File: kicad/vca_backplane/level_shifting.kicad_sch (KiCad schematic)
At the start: 10 parts, among them Q3 BSS138, Q4 BSS138, U2 74HCT245, U3 74LVC245

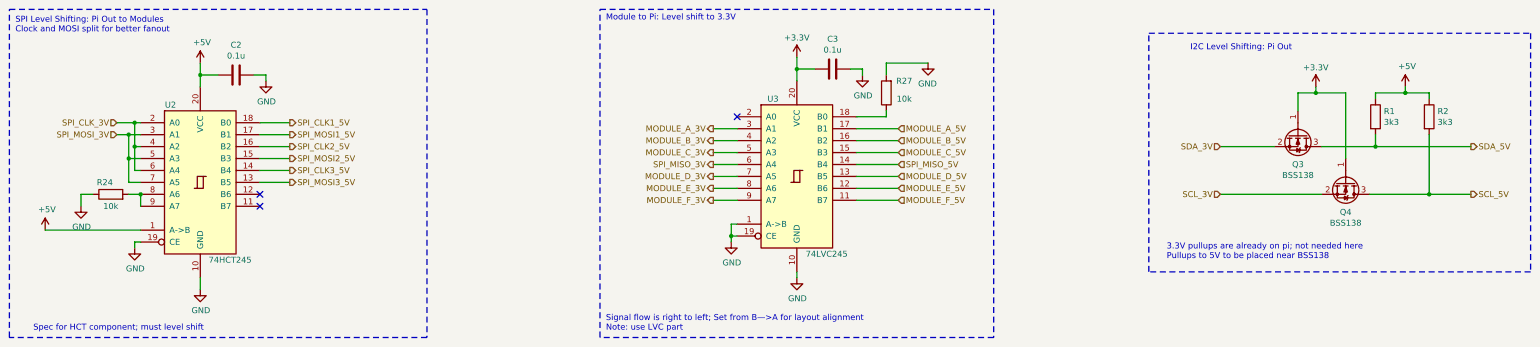
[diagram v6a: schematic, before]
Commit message: geographically reorientated from pcb
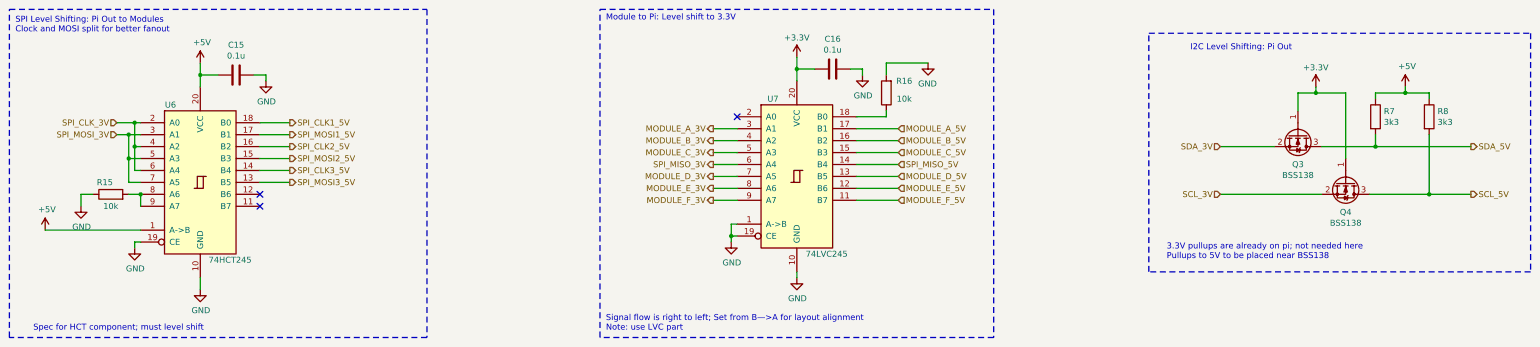
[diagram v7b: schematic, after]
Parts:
- renumbered C2 to C15, C3 to C16, R24 to R15, R27 to R16, R1 to R7, R2 to R8, U2 to U6, U3 to U7
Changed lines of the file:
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@@
   (symbol (lib_id "Device:C") (at 77.47 55.88 270) (unit 1)
     (in_bom yes) (on_board yes) (dnp no)
-    (property "Reference" "C2" (at 77.47 49.4792 90)
+    (property "Reference" "C15" (at 77.47 49.4792 90)
       (effects (font (size 1.27 1.27)))
     )
@@
       (project "vca_backplane"
         (path "/bdbd6910-8f28-459f-89ba-e6dd447d59a9/00000000-0000-0000-0000-00006255a619"
-          (reference "C2") (unit 1)
+          (reference "C15") (unit 1)
         )
       )
@@
   (symbol (lib_id "74xx:74HC245") (at 69.85 78.74 0) (unit 1)
     (in_bom yes) (on_board yes) (dnp no)
-    (property "Reference" "U2" (at 63.5 62.23 0)
+    (property "Reference" "U6" (at 63.5 62.23 0)
       (effects (font (size 1.27 1.27)))
     )
@@
       (project "vca_backplane"
         (path "/bdbd6910-8f28-459f-89ba-e6dd447d59a9/00000000-0000-0000-0000-00006255a619"
-          (reference "U2") (unit 1)
+          (reference "U6") (unit 1)
         )
       )
@@
   (symbol (lib_id "Device:R") (at 320.04 64.77 0) (unit 1)
     (in_bom yes) (on_board yes) (dnp no)
-    (property "Reference" "R1" (at 321.818 63.6016 0)
+    (property "Reference" "R7" (at 321.818 63.6016 0)
       (effects (font (size 1.27 1.27)) (justify left))
     )
@@
       (project "vca_backplane"
         (path "/bdbd6910-8f28-459f-89ba-e6dd447d59a9/00000000-0000-0000-0000-00006255a619"
-          (reference "R1") (unit 1)
+          (reference "R7") (unit 1)
         )
       )
@@
   (symbol (lib_id "Device:R") (at 331.47 64.77 0) (unit 1)
     (in_bom yes) (on_board yes) (dnp no)
-    (property "Reference" "R2" (at 333.248 63.6016 0)
+    (property "Reference" "R8" (at 333.248 63.6016 0)
       (effects (font (size 1.27 1.27)) (justify left))
     )
@@
       (project "vca_backplane"
         (path "/bdbd6910-8f28-459f-89ba-e6dd447d59a9/00000000-0000-0000-0000-00006255a619"
-          (reference "R2") (unit 1)
+          (reference "R8") (unit 1)
         )
       )
@@
   (symbol (lib_id "74xx:74HC245") (at 196.85 77.47 0) (unit 1)
     (in_bom yes) (on_board yes) (dnp no)
-    (property "Reference" "U3" (at 191.77 60.96 0)
+    (property "Reference" "U7" (at 191.77 60.96 0)
       (effects (font (size 1.27 1.27)))
     )
@@
       (project "vca_backplane"
         (path "/bdbd6910-8f28-459f-89ba-e6dd447d59a9/00000000-0000-0000-0000-00006255a619"
-          (reference "U3") (unit 1)
+          (reference "U7") (unit 1)
         )
       )
@@
   (symbol (lib_id "Device:C") (at 204.47 54.61 270) (unit 1)
     (in_bom yes) (on_board yes) (dnp no)
-    (property "Reference" "C3" (at 204.47 48.2092 90)
+    (property "Reference" "C16" (at 204.47 48.2092 90)
       (effects (font (size 1.27 1.27)))
     )
@@
       (project "vca_backplane"
         (path "/bdbd6910-8f28-459f-89ba-e6dd447d59a9/00000000-0000-0000-0000-00006255a619"
-          (reference "C3") (unit 1)
+          (reference "C16") (unit 1)
         )
       )
@@
   (symbol (lib_id "Device:R") (at 215.9 59.69 180) (unit 1)
     (in_bom yes) (on_board yes) (dnp no)
-    (property "Reference" "R27" (at 219.71 57.15 0)
+    (property "Reference" "R16" (at 219.71 57.15 0)
       (effects (font (size 1.27 1.27)))
     )
@@
       (project "vca_backplane"
         (path "/bdbd6910-8f28-459f-89ba-e6dd447d59a9/00000000-0000-0000-0000-00006255a619"
-          (reference "R27") (unit 1)
+          (reference "R16") (unit 1)
         )
       )
@@
   (symbol (lib_id "Device:R") (at 50.8 81.28 90) (unit 1)
     (in_bom yes) (on_board yes) (dnp no)
-    (property "Reference" "R24" (at 49.53 78.74 90)
+    (property "Reference" "R15" (at 49.53 78.74 90)
       (effects (font (size 1.27 1.27)))
     )
@@
       (project "vca_backplane"
         (path "/bdbd6910-8f28-459f-89ba-e6dd447d59a9/00000000-0000-0000-0000-00006255a619"
-          (reference "R24") (unit 1)
-        )
-      )
+          (reference "R15") (unit 1)
+        )
+      )
